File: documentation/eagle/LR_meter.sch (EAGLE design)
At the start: 15 parts, among them IC1 LM393N, X1 22-23-2051

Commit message: Updating design :
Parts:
- removed INDUCTORTEST, RESISTORTEST2: 0, con-wago-500:W237-102
- removed X1: 22-23-2051, con-molex:22-23-2051
- added J1: Inductor test terminal, SparkFun-Connectors:CONN_02
- added J2: Resistor test terminal, SparkFun-Connectors:CONN_02
- added J3: Joystick, SparkFun-Connectors:CONN_05
- R1: value 1K -> 10K
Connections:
- removed net 5V: IC1P.V+, R7.1, U$1.5.5V, X1-1.S
- removed net N$2: U$1.A0, X1-2.S
- removed net N$3: U$1.A1, X1-3.S
- removed net N$4: R1.1, U$1.D2, X1-4.S
- removed net N$5: U$1.GND2, X1-5.S
- new net MS: J3.1, R1.1, U$1.D2
- new net VCC: IC1P.V+, J3.4, R1.2, R7.1, U$1.5.5V
- new net VRX: J3.3, U$1.A0
- new net VRY: J3.2, U$1.A1
- net GND: now also J1.1, J3.5; no longer INDUCTORTEST-2.KL, R1.2
- net N$11: now also J2.2; no longer RESISTORTEST2-2.KL
- net N$13: now also J1.2; no longer INDUCTORTEST-1.KL
- net N$30: now also J2.1; no longer RESISTORTEST2-1.KL
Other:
- note removed: "joystick"
- moved on the sheet: C1, R3

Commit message: Version 1.1-2
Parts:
- removed C1: 1uF, capacitor-wima:C5/2.5
- added J4: LCD 1602 I2C, SparkFun-Connectors:I2C_STANDARD
- C2: value 1uF -> 2uF
- D1: value 1N4148DO35-10 -> 1N4148
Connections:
- new net N$1: J4.4, U$1.A5
- new net N$2: J4.3, U$1.A4
- net GND: now also J4.1; no longer C1.2
- net N$13: no longer C1.1
- net N$15: now also R7.1; no longer R7.2
- net VCC: now also J4.2, R7.2; no longer R7.1
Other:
- moved on the sheet: D1, R6, R7

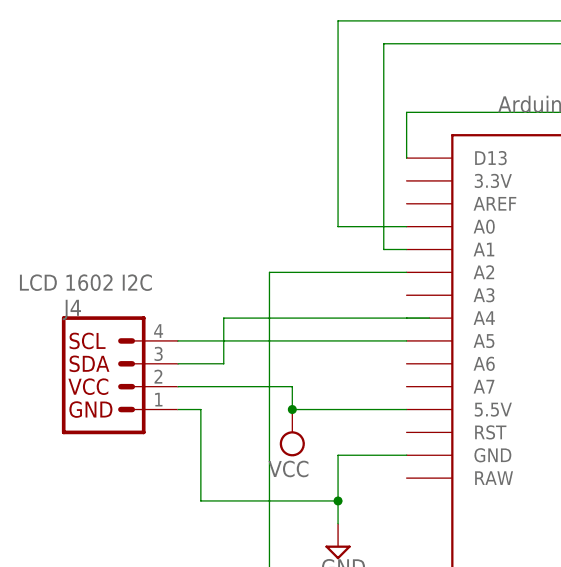
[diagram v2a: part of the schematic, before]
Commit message: version 1.1-2, adding OLED
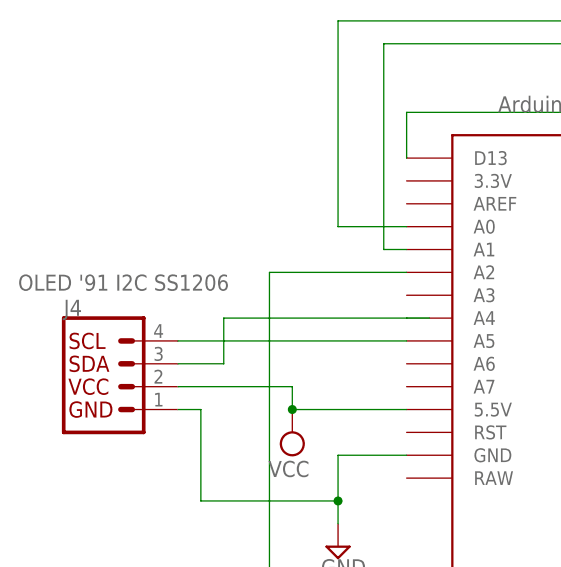
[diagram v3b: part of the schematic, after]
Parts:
- J4: value LCD 1602 I2C -> OLED '91 I2C SS1206
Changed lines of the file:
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@@
 <part name="SUPPLY6" library="supply2" library_urn="urn:adsk.eagle:library:372" deviceset="VCC" device=""/>
 <part name="SUPPLY7" library="supply2" library_urn="urn:adsk.eagle:library:372" deviceset="VCC" device=""/>
-<part name="J4" library="SparkFun-Connectors" library_urn="urn:adsk.eagle:library:513" deviceset="I2C_STANDARD" device="" package3d_urn="urn:adsk.eagle:package:38085/1" value="LCD 1602 I2C"/>
+<part name="J4" library="SparkFun-Connectors" library_urn="urn:adsk.eagle:library:513" deviceset="I2C_STANDARD" device="" package3d_urn="urn:adsk.eagle:package:38085/1" value="OLED '91 I2C SS1206"/>
 </parts>
 <sheets>

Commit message: version 2.0
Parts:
- removed R1: 10K, eagle-ltspice:R0207/10
- added J5: (no value), SparkFun-Connectors:CONN_031X03_SMD_RA_MALE_POST_SMALLEST
- added S1: SPST Mode button, SparkFun-Switches:MOMENTARY-SWITCH-SPST-PTH-6.0MM-KIT
- added S2: SPST Test Button, SparkFun-Switches:MOMENTARY-SWITCH-SPST-PTH-6.0MM-KIT
- IC1: value LM393N -> LM339
- J1: value Inductor test terminal -> (none)
- J2: value Resistor test terminal -> (none)
- J3: value Joystick -> (none); device SparkFun-Connectors:CONN_05 -> SparkFun-Connectors:CONN_031X03_SMD_RA_MALE_POST_SMALLEST
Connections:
- removed net MS: J3.1, R1.1, U$1.D2
- removed net VRY: J3.2, U$1.A1
- new net N$10: S1.2
- new net N$16: S2.2
- new net N$3: U$1.D5
- new net N$4: U$1.D6
- new net N$5: U$1.D4
- net GND: now also J3.3, J5.3, S1.1, S2.1; no longer J3.5
- net N$12: now also U$1.A2; no longer R6.1, U$1.D13
- net N$30: no longer U$1.A2
- net VCC: now also J3.1, J5.1; no longer J3.4, R1.2
- net VRX: now also J3.2, J5.2; no longer J3.3
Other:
- note added: "Analog Test Terminal"
- note added: "Inductor test terminal"
- note added: "Resistor test terminal"

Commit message: version 2.1-2
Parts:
- added R1: 4.7k, eagle-ltspice:R0207/10
- added R8: 4.7K, eagle-ltspice:R0207/10
- IC1: value LM339 -> LM393
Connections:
- net N$1: now also R1.1
- net N$2: now also R8.1
- net VCC: now also R1.2, R8.2
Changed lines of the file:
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@@
 <?xml version="1.0" encoding="utf-8"?>
 <!DOCTYPE eagle SYSTEM "eagle.dtd">
-<eagle version="9.3.0">
+<eagle version="9.3.1">
 <drawing>
 <settings>
@@
 <part name="C2" library="capacitor-wima" library_urn="urn:adsk.eagle:library:116" deviceset="C" device="5/2.5" package3d_urn="urn:adsk.eagle:package:5426/1" value="2uF"/>
 <part name="R7" library="resistor" library_urn="urn:adsk.eagle:library:348" deviceset="R-EU_" device="0207/15" package3d_urn="urn:adsk.eagle:package:25947/1" value="330"/>
-<part name="IC1" library="linear" library_urn="urn:adsk.eagle:library:262" deviceset="LM393" device="N" package3d_urn="urn:adsk.eagle:package:16409/2" value="LM339"/>
+<part name="IC1" library="linear" library_urn="urn:adsk.eagle:library:262" deviceset="LM393" device="N" package3d_urn="urn:adsk.eagle:package:16409/2" value="LM393"/>
 <part name="SUPPLY1" library="supply2" library_urn="urn:adsk.eagle:library:372" deviceset="GND" device=""/>
 <part name="SUPPLY2" library="supply2" library_urn="urn:adsk.eagle:library:372" deviceset="GND" device=""/>
@@
 <part name="S2" library="SparkFun-Switches" library_urn="urn:adsk.eagle:library:535" deviceset="MOMENTARY-SWITCH-SPST" device="-PTH-6.0MM-KIT" package3d_urn="urn:adsk.eagle:package:40170/1" value="SPST Test Button"/>
 <part name="SUPPLY6" library="supply2" library_urn="urn:adsk.eagle:library:372" deviceset="GND" device=""/>
+<part name="R1" library="eagle-ltspice" library_urn="urn:adsk.eagle:library:217" deviceset="R" device="0207/10" package3d_urn="urn:adsk.eagle:package:13275/1" value="4.7k"/>
+<part name="R8" library="eagle-ltspice" library_urn="urn:adsk.eagle:library:217" deviceset="R" device="0207/10" package3d_urn="urn:adsk.eagle:package:13275/1" value="4.7K"/>
+<part name="SUPPLY8" library="supply2" library_urn="urn:adsk.eagle:library:372" deviceset="VCC" device=""/>
 </parts>
 <sheets>
@@
 </instance>
 <instance part="J4" gate="G$1" x="-45.72" y="48.26" smashed="yes">
-<attribute name="VALUE" x="-55.88" y="60.706" size="1.778" layer="96" font="vector" align="top-left"/>
+<attribute name="VALUE" x="-55.88" y="37.846" size="1.778" layer="96" font="vector" rot="R90" align="top-left"/>
 <attribute name="NAME" x="-50.8" y="56.134" size="1.778" layer="95" font="vector"/>
 </instance>
@@
 <instance part="SUPPLY6" gate="GND" x="27.94" y="109.22" smashed="yes" rot="R180">
 <attribute name="VALUE" x="29.845" y="112.395" size="1.778" layer="96" rot="R180"/>
+</instance>
+<instance part="R1" gate="G$1" x="-38.1" y="88.9" smashed="yes" rot="R90">
+<attribute name="NAME" x="-39.5986" y="85.09" size="1.778" layer="95" rot="R90"/>
+<attribute name="VALUE" x="-39.878" y="92.71" size="1.778" layer="96" rot="R90"/>
+</instance>
+<instance part="R8" gate="G$1" x="-35.56" y="88.9" smashed="yes" rot="R90">
+<attribute name="NAME" x="-31.9786" y="92.71" size="1.778" layer="95" rot="R90"/>
+<attribute name="VALUE" x="-32.258" y="85.09" size="1.778" layer="96" rot="R90"/>
+</instance>
+<instance part="SUPPLY8" gate="G$1" x="-38.1" y="104.14" smashed="yes">
+<attribute name="VALUE" x="-40.005" y="107.315" size="1.778" layer="96"/>
 </instance>
 </instances>
@@
 <pinref part="SUPPLY3" gate="G$1" pin="VCC"/>
 </segment>
+<segment>
+<pinref part="R8" gate="G$1" pin="2"/>
+<wire x1="-35.56" y1="93.98" x2="-35.56" y2="101.6" width="0.1524" layer="91"/>
+<wire x1="-35.56" y1="101.6" x2="-38.1" y2="101.6" width="0.1524" layer="91"/>
+<wire x1="-38.1" y1="101.6" x2="-38.1" y2="93.98" width="0.1524" layer="91"/>
+<pinref part="R1" gate="G$1" pin="2"/>
+<pinref part="SUPPLY8" gate="G$1" pin="VCC"/>
+<junction x="-38.1" y="101.6"/>
+</segment>
 </net>
 <net name="VRX" class="0">
@@
 <pinref part="U$1" gate="G$1" pin="A5"/>
 <wire x1="-38.1" y1="53.34" x2="-12.7" y2="53.34" width="0.1524" layer="91"/>
+<wire x1="-38.1" y1="53.34" x2="-38.1" y2="83.82" width="0.1524" layer="91"/>
+<junction x="-38.1" y="53.34"/>
+<pinref part="R1" gate="G$1" pin="1"/>
 </segment>
 </net>
@@
 <wire x1="-33.02" y1="55.88" x2="-33.02" y2="50.8" width="0.1524" layer="91"/>
 <pinref part="J4" gate="G$1" pin="3"/>
-<wire x1="-33.02" y1="50.8" x2="-38.1" y2="50.8" width="0.1524" layer="91"/>
-</segment>
-</net>
+<wire x1="-33.02" y1="50.8" x2="-35.56" y2="50.8" width="0.1524" layer="91"/>
+<wire x1="-35.56" y1="50.8" x2="-38.1" y2="50.8" width="0.1524" layer="91"/>
+<wire x1="-35.56" y1="50.8" x2="-35.56" y2="83.82" width="0.1524" layer="91"/>
+<junction x="-35.56" y="50.8"/>
+<pinref part="R8" gate="G$1" pin="1"/>
+</segment>
+</net>
